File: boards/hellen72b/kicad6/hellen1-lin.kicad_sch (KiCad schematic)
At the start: 6 parts

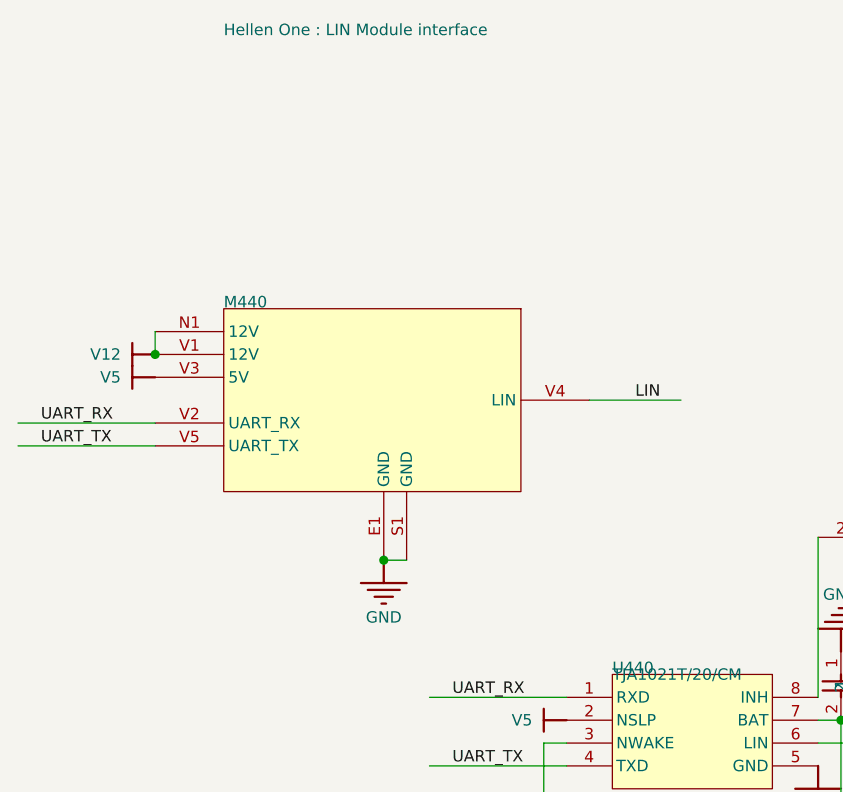
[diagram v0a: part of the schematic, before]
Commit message: update after refactoring can,lin,sd,stlink
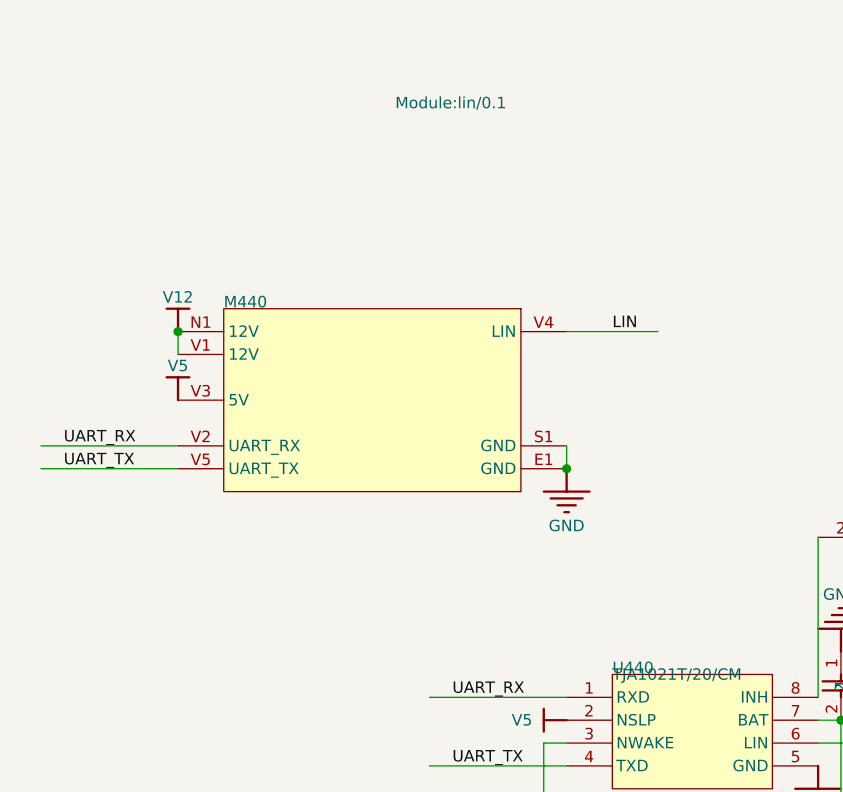
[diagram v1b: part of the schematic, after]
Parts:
- M440: Comment Hellen One : LIN Module interface -> Module:lin/0.1
